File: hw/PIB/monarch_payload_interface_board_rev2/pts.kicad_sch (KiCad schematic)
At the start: 16 parts, among them U9 AD7124-8BCPZ-RL

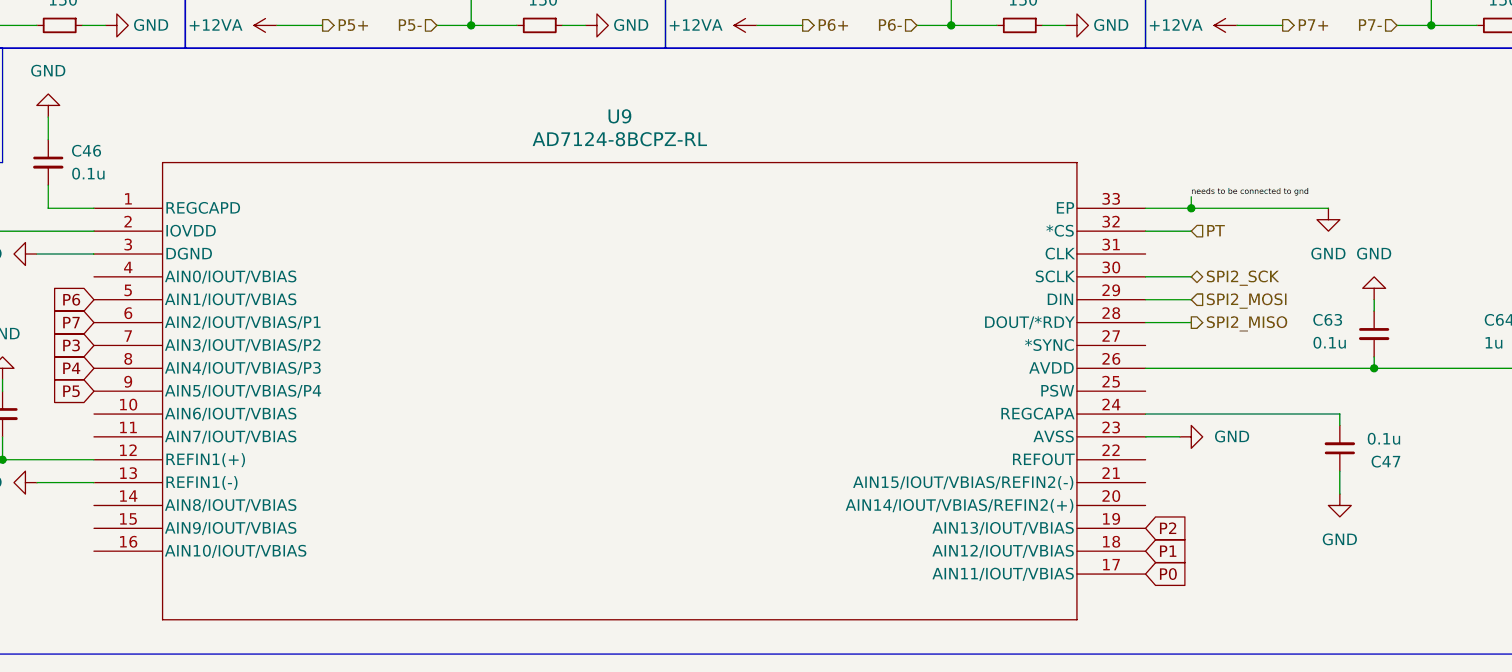
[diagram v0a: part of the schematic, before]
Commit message: Schematic Clean Up + New Micro-Lock Plus Connectors
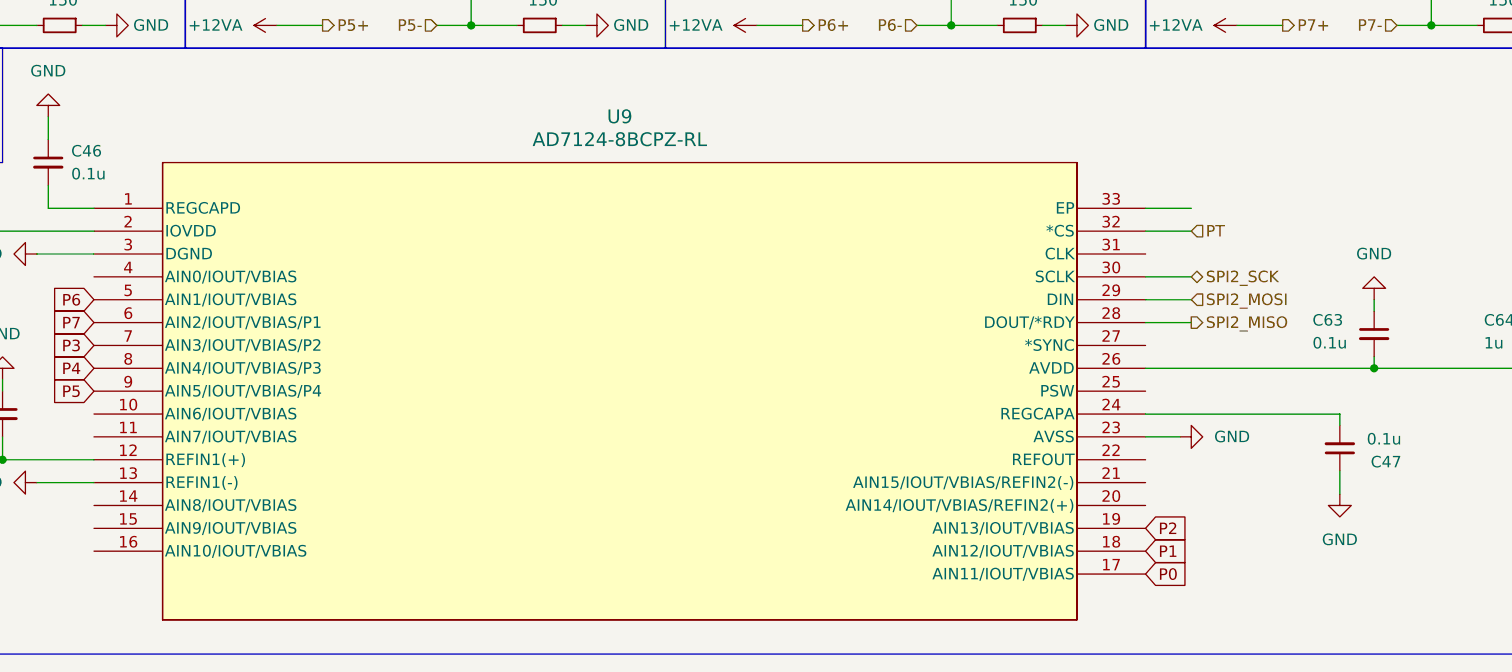
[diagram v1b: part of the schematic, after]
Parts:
- U9: footprint AD7124:CP-32-12_ADI-L -> CP-32-12_ADI
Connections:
- net GND: no longer U9.33 (EP)
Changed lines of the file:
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@@
 	)
 	(junction
-		(at 204.47 60.96)
-		(diameter 0)
-		(color 0 0 0 0)
-	)
-	(junction
 		(at 231.14 40.64)
 		(diameter 0)
@@
 	(wire
 		(pts
-			(xy 204.47 59.69) (xy 204.47 60.96)
-		)
-		(stroke
-			(width 0)
-			(type default)
-		)
-	)
-	(wire
-		(pts
 			(xy 231.14 25.4) (xy 231.14 30.48)
 		)
@@
 	(wire
 		(pts
-			(xy 204.47 60.96) (xy 219.71 60.96)
-		)
-		(stroke
-			(width 0)
-			(type default)
-		)
-	)
-	(wire
-		(pts
 			(xy 67.31 30.48) (xy 71.12 30.48)
 		)
@@
 		)
 	)
-	(label "needs to be connected to gnd"
-		(at 204.47 59.69 0)
-		(effects
-			(font
-				(size 0.635 0.635)
-			)
-			(justify left bottom)
-		)
-	)
 	(global_label "P7"
 		(shape input)
@@
 	)
 	(symbol
-		(lib_id "power:GND")
-		(at 219.71 60.96 0)
-		(unit 1)
-		(body_style 1)
-		(exclude_from_sim no)
-		(in_bom yes)
-		(on_board yes)
-		(in_pos_files yes)
-		(dnp no)
-		(fields_autoplaced yes)
-		(property "Reference" "#PWR03"
-			(at 219.71 67.31 0)
-			(hide yes)
-			(show_name no)
-			(do_not_autoplace no)
-			(effects
-				(font
-					(size 1.27 1.27)
-				)
-			)
-		)
-		(property "Value" "GND"
-			(at 219.71 66.04 0)
-			(show_name no)
-			(do_not_autoplace no)
-			(effects
-				(font
-					(size 1.27 1.27)
-				)
-			)
-		)
-		(property "Footprint" ""
-			(at 219.71 60.96 0)
-			(hide yes)
-			(show_name no)
-			(do_not_autoplace no)
-			(effects
-				(font
-					(size 1.27 1.27)
-				)
-			)
-		)
-		(property "Datasheet" ""
-			(at 219.71 60.96 0)
-			(hide yes)
-			(show_name no)
-			(do_not_autoplace no)
-			(effects
-				(font
-					(size 1.27 1.27)
-				)
-			)
-		)
-		(property "Description" "Power symbol creates a global label with name \"GND\" , ground"
-			(at 219.71 60.96 0)
-			(hide yes)
-			(show_name no)
-			(do_not_autoplace no)
-			(effects
-				(font
-					(size 1.27 1.27)
-				)
-			)
-		)
-		(pin "1"
-		)
-		(instances
-			(project "monarch_payload_interface_board_rev2"
-				(path "/bf7ee58d-ac53-49d1-a6b2-96a87d67b737/dd3c8404-7b7b-4e20-8fce-52b620531aa5"
-					(reference "#PWR03")
-					(unit 1)
-				)
-			)
-		)
-	)
-	(symbol
 		(lib_id "power:+3V3")
 		(at 248.92 78.74 270)
@@
 			)
 		)
-		(property "Footprint" "AD7124:CP-32-12_ADI-L"
+		(property "Footprint" "CP-32-12_ADI"
 			(at 82.55 60.96 0)
 			(hide yes)

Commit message: AD7124 Fixes
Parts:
- added C70: 0.1u, Capacitor_SMD:C_0603_1608Metric, symbol Device:C_Small
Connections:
- net +3V3: now also C70.1
- net GND: now also U9.33 (EP), C70.2
- no-connect marks 0 -> 10

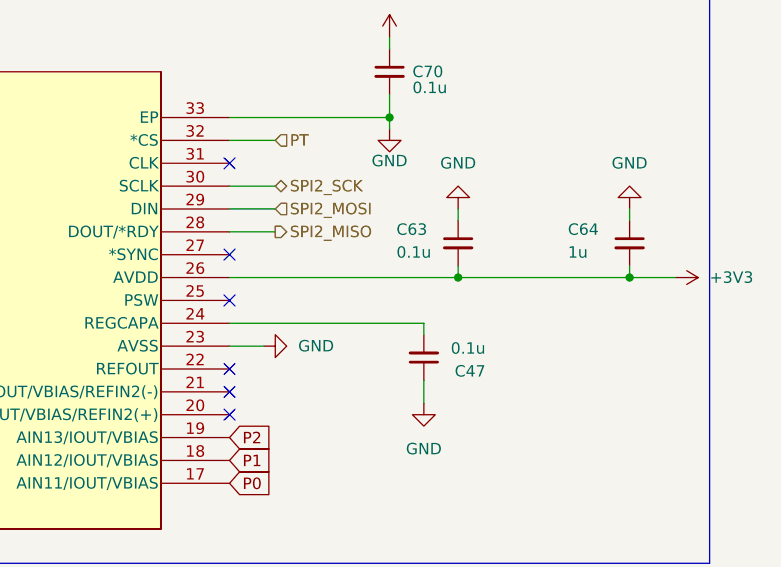
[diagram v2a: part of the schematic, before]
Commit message: Connector Footprints / Additions + Validated MAX31856
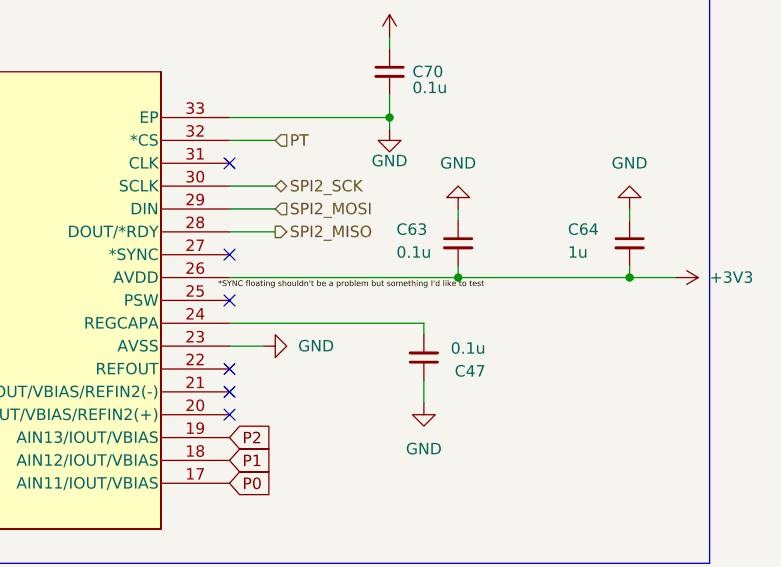
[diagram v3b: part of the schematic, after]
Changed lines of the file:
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@@
+		)
+	)
+	(label "*SYNC floating shouldn't be a problem but something I'd like to test"
+		(at 198.12 80.01 0)
+		(effects
+			(font
+				(size 0.635 0.635)
+			)
+			(justify left bottom)
 		)
 	)

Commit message: AD7124 fixes
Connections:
- net GND is gone; now on net +12VA: C46.1, C47.1, C60.1, C61.1, C62.1, C63.1, C64.1, C70.2, R32.1, R33.1, R34.1, R35.1, R36.1, R37.1, R38.1, R39.1, U9.13 (REFIN1(-)), U9.23 (AVSS), U9.3 (DGND), U9.33 (EP)
- net +12VA: now also R39.2, U9.4 (AIN0/IOUT/VBIAS), U9.5 (AIN1/IOUT/VBIAS)
- net P0: no longer R39.2
- net P6: no longer U9.5 (AIN1/IOUT/VBIAS)
- no-connect marks 10 -> 9
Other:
- moved on the sheet: R37, R39
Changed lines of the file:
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@@
 	)
 	(junction
-		(at 177.8 30.48)
+		(at 82.55 30.48)
 		(diameter 0)
 		(color 0 0 0 0)
 	)
 	(junction
-		(at 243.84 78.74)
+		(at 177.8 30.48)
 		(diameter 0)
 		(color 0 0 0 0)
 	)
 	(junction
-		(at 71.12 40.64)
+		(at 243.84 78.74)
 		(diameter 0)
 		(color 0 0 0 0)
@@
 	)
 	(junction
-		(at 124.46 40.64)
+		(at 71.12 40.64)
 		(diameter 0)
 		(color 0 0 0 0)
 	)
 	(junction
-		(at 71.12 30.48)
+		(at 124.46 40.64)
 		(diameter 0)
 		(color 0 0 0 0)
@@
 	)
 	(junction
+		(at 71.12 30.48)
+		(diameter 0)
+		(color 0 0 0 0)
+	)
+	(junction
 		(at 231.14 40.64)
 		(diameter 0)
@@
 	)
 	(no_connect
-		(at 82.55 68.58)
-	)
-	(no_connect
 		(at 82.55 96.52)
 	)
@@
 	(wire
 		(pts
+			(xy 82.55 30.48) (xy 83.82 30.48)
+		)
+		(stroke
+			(width 0)
+			(type default)
+		)
+	)
+	(wire
+		(pts
 			(xy 243.84 78.74) (xy 248.92 78.74)
 		)
@@
 	(wire
 		(pts
+			(xy 82.55 25.4) (xy 82.55 30.48)
+		)
+		(stroke
+			(width 0)
+			(type default)
+		)
+	)
+	(wire
+		(pts
 			(xy 199.39 68.58) (xy 204.47 68.58)
 		)
@@
 	(wire
 		(pts
-			(xy 71.12 30.48) (xy 76.2 30.48)
+			(xy 71.12 30.48) (xy 74.93 30.48)
 		)
 		(stroke
@@
 	(wire
 		(pts
-			(xy 81.28 30.48) (xy 83.82 30.48)
+			(xy 80.01 30.48) (xy 82.55 30.48)
 		)
 		(stroke
@@
 	(wire
 		(pts
-			(xy 71.12 40.64) (xy 76.2 40.64)
+			(xy 71.12 40.64) (xy 74.93 40.64)
 		)
 		(stroke
@@
 	(wire
 		(pts
-			(xy 81.28 40.64) (xy 83.82 40.64)
+			(xy 80.01 40.64) (xy 83.82 40.64)
 		)
 		(stroke
@@
 		)
 	)
+	(global_label "P0-"
+		(shape input)
+		(at 82.55 25.4 0)
+		(fields_autoplaced yes)
+		(effects
+			(font
+				(size 1.27 1.27)
+			)
+			(justify left)
+		)
+		(property "Intersheetrefs" "${INTERSHEET_REFS}"
+			(at 88.9329 25.4 0)
+			(hide yes)
+			(show_name no)
+			(do_not_autoplace no)
+			(effects
+				(font
+					(size 1.27 1.27)
+				)
+				(justify left)
+			)
+		)
+	)
 	(global_label "P1"
 		(shape input)
@@
 		)
 	)
+	(global_label "P0+"
+		(shape input)
+		(at 82.55 68.58 180)
+		(fields_autoplaced yes)
+		(effects
+			(font
+				(size 1.27 1.27)
+			)
+			(justify right)
+		)
+		(property "Intersheetrefs" "${INTERSHEET_REFS}"
+			(at 76.1671 68.58 0)
+			(hide yes)
+			(show_name no)
+			(do_not_autoplace no)
+			(effects
+				(font
+					(size 1.27 1.27)
+				)
+				(justify right)
+			)
+		)
+	)
 	(global_label "P6"
 		(shape input)
-		(at 82.55 71.12 180)
+		(at 76.2 71.12 180)
 		(fields_autoplaced yes)
 		(effects
@@
 		)
 		(property "Intersheetrefs" "${INTERSHEET_REFS}"
-			(at 77.0853 71.12 0)
+			(at 70.7353 71.12 0)
 			(hide yes)
 			(show_name no)
@@
 		)
 	)
-	(global_label "P0"
+	(global_label "P0-"
+		(shape input)
+		(at 82.55 71.12 180)
+		(fields_autoplaced yes)
+		(effects
+			(font
+				(size 1.27 1.27)
+			)
+			(justify right)
+		)
+		(property "Intersheetrefs" "${INTERSHEET_REFS}"
+			(at 76.1671 71.12 0)
+			(hide yes)
+			(show_name no)
+			(do_not_autoplace no)
+			(effects
+				(font
+					(size 1.27 1.27)
+				)
+				(justify right)
+			)
+		)
+	)
+	(global_label "P0+"
 		(shape input)
 		(at 71.12 25.4 180)
@@
 		)
 		(property "Intersheetrefs" "${INTERSHEET_REFS}"
-			(at 65.6553 25.4 0)
+			(at 64.7371 25.4 0)
 			(hide yes)
 			(show_name no)
@@
 	(symbol
 		(lib_id "Device:R_Small")
-		(at 78.74 30.48 270)
+		(at 77.47 30.48 270)
 		(unit 1)
 		(body_style 1)
@@
 		(dnp no)
 		(property "Reference" "R39"
-			(at 80.264 25.4 90)
+			(at 78.994 25.4 90)
 			(show_name no)
 			(do_not_autoplace no)
@@
 		)
 		(property "Value" "150"
-			(at 80.772 27.686 90)
+			(at 79.502 27.686 90)
 			(show_name no)
 			(do_not_autoplace no)
@@
 		)
 		(property "Footprint" "Resistor_SMD:R_0603_1608Metric"
-			(at 78.74 30.48 0)
+			(at 77.47 30.48 0)
 			(hide yes)
 			(show_name no)
@@
 		)
 		(property "Datasheet" ""
-			(at 78.74 30.48 0)
+			(at 77.47 30.48 0)
 			(hide yes)
 			(show_name no)
@@
 		)
 		(property "Description" "Resistor, small symbol"
-			(at 78.74 30.48 0)
+			(at 77.47 30.48 0)
 			(hide yes)
 			(show_name no)
@@
 	(symbol
 		(lib_id "Device:R_Small")
-		(at 78.74 40.64 270)
+		(at 77.47 40.64 270)
 		(unit 1)
 		(body_style 1)
@@
 		(dnp no)
 		(property "Reference" "R37"
-			(at 80.264 35.56 90)
+			(at 78.994 35.56 90)
 			(show_name no)
 			(do_not_autoplace no)
@@
 		)
 		(property "Value" "150"
-			(at 80.772 37.846 90)
+			(at 79.502 37.846 90)
 			(show_name no)
 			(do_not_autoplace no)
@@
 		)
 		(property "Footprint" "Resistor_SMD:R_0603_1608Metric"
-			(at 78.74 40.64 0)
+			(at 77.47 40.64 0)
 			(hide yes)
 			(show_name no)
@@
 		)
 		(property "Datasheet" ""
-			(at 78.74 40.64 0)
+			(at 77.47 40.64 0)
 			(hide yes)
 			(show_name no)
@@
 		)
 		(property "Description" "Resistor, small symbol"
-			(at 78.74 40.64 0)
+			(at 77.47 40.64 0)
 			(hide yes)
 			(show_name no)

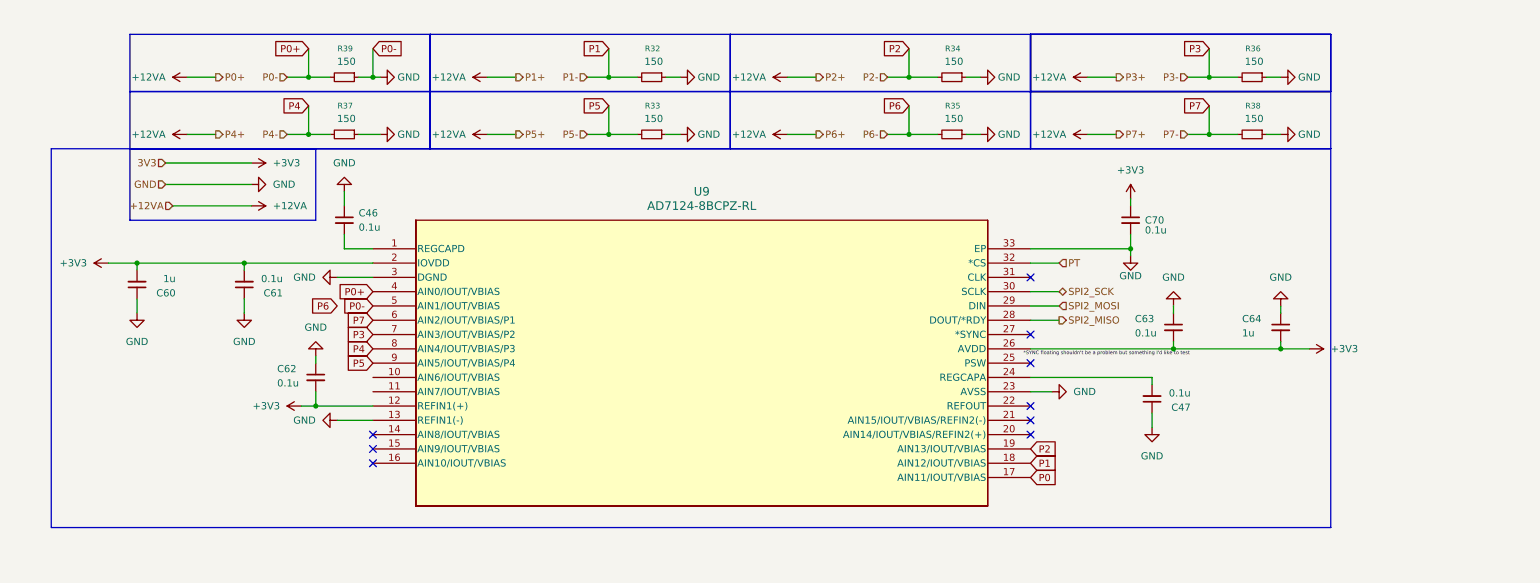
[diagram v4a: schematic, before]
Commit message: Schematic Updates Finished -> AD7124 Voltage Reading Fix + Connector Linkage Issue Fix
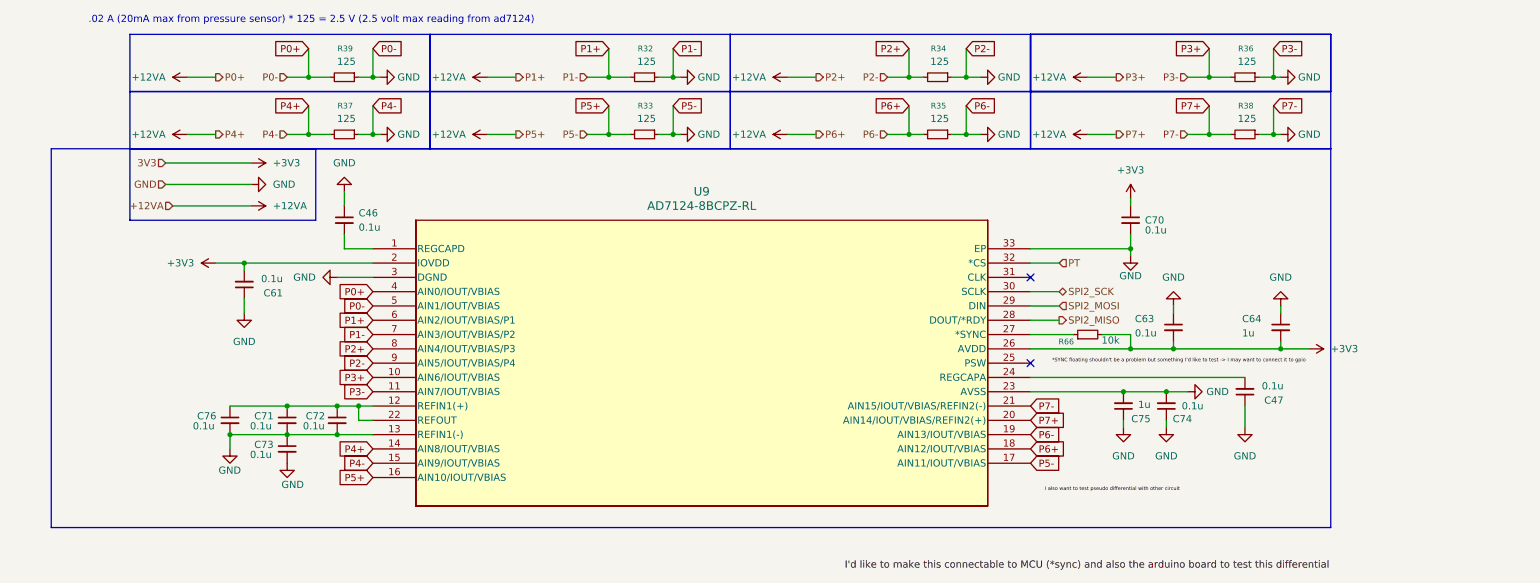
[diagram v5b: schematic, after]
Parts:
- removed C60: 1u, Capacitor_SMD:C_0603_1608Metric, symbol Device:C_Small
- removed C62: 0.1u, Capacitor_SMD:C_0603_1608Metric, symbol Device:C_Small
- added C71, C72, C73, C74, C76: 0.1u, Capacitor_SMD:C_0603_1608Metric, symbol Device:C_Small
- added C75: 1u, Capacitor_SMD:C_0603_1608Metric, symbol Device:C_Small
- added R66: 10k, Resistor_SMD:R_0603_1608Metric, symbol Device:R_Small
- R32, R33, R34, R35, R36, R37, R38, R39: value 150 -> 125
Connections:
- net P0 is gone; now on net +12VA: U9.17 (AIN11/IOUT/VBIAS)
- net P1 is gone; now on net +12VA: R32.2, U9.18 (AIN12/IOUT/VBIAS)
- net P2 is gone; now on net +12VA: R34.2, U9.19 (AIN13/IOUT/VBIAS)
- net P3 is gone; now on net +12VA: R36.2, U9.7 (AIN3/IOUT/VBIAS/P2)
- net P4 is gone; now on net +12VA: R37.2, U9.8 (AIN4/IOUT/VBIAS/P3)
- net P5 is gone; now on net +12VA: R33.2, U9.9 (AIN5/IOUT/VBIAS/P4)
- net P6 is gone; now on net +12VA: R35.2
- net P7 is gone; now on net +12VA: R38.2, U9.6 (AIN2/IOUT/VBIAS/P1)
- net +12VA: now also U9.10 (AIN6/IOUT/VBIAS), U9.11 (AIN7/IOUT/VBIAS), U9.14 (AIN8/IOUT/VBIAS), U9.15 (AIN9/IOUT/VBIAS), U9.16 (AIN10/IOUT/VBIAS), U9.20 (AIN14/IOUT/VBIAS/REFIN2(+)), U9.21 (AIN15/IOUT/VBIAS/REFIN2(-)), C71.2, C72.2, C73.1, C73.2, C74.1, C74.2, C75.1, C75.2, C76.2
- net +3V3: now also R66.2; no longer U9.12 (REFIN1(+))
- net at U9.22 (REFOUT): now also U9.12 (REFIN1(+)), C71.1, C72.1, C76.1
- net at U9.27 (*SYNC): now also R66.1
- no-connect marks 9 -> 2
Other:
- note added: ".02 A (20mA max from pressure sensor) * 125 = 2.5 V (2.5 volt max reading from ad7124)"
- moved on the sheet: C47, R32, R33, R34, R35, R36, R38

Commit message: Footprint Selected
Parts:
- U9: footprint CP-32-12_ADI -> AD7124:CP-32-12_ADI
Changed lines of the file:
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@@
 			)
 		)
-		(property "Footprint" "CP-32-12_ADI"
+		(property "Footprint" "AD7124:CP-32-12_ADI"
 			(at 82.55 60.96 0)
 			(hide yes)

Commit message: Initial Routing Work + Placement
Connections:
- net +12VA: no longer C46.1, C47.1, C61.1, C63.1, C64.1, C70.2, C71.2, C72.2, C73.1, C73.2, C74.1, C74.2, C75.1, C75.2, C76.2, R32.1, R32.2, R33.1, R33.2, R34.1, R34.2, R35.1, R35.2, R36.1, R36.2, R37.1, R37.2, R38.1, R38.2, R39.1, R39.2, U9.10 (AIN6/IOUT/VBIAS), U9.11 (AIN7/IOUT/VBIAS), U9.13 (REFIN1(-)), U9.14 (AIN8/IOUT/VBIAS), U9.15 (AIN9/IOUT/VBIAS), U9.16 (AIN10/IOUT/VBIAS), U9.17 (AIN11/IOUT/VBIAS), U9.18 (AIN12/IOUT/VBIAS), U9.19 (AIN13/IOUT/VBIAS), U9.20 (AIN14/IOUT/VBIAS/REFIN2(+)), U9.21 (AIN15/IOUT/VBIAS/REFIN2(-)), U9.23 (AVSS), U9.3 (DGND), U9.33 (EP), U9.4 (AIN0/IOUT/VBIAS), U9.5 (AIN1/IOUT/VBIAS), U9.6 (AIN2/IOUT/VBIAS/P1), U9.7 (AIN3/IOUT/VBIAS/P2), U9.8 (AIN4/IOUT/VBIAS/P3), U9.9 (AIN5/IOUT/VBIAS/P4)
- new net GND: C46.1, C47.1, C61.1, C63.1, C64.1, C70.2, C71.2, C72.2, C73.1, C73.2, C74.1, C74.2, C75.1, C75.2, C76.2, R32.1, R33.1, R34.1, R35.1, R36.1, R37.1, R38.1, R39.1, U9.11 (AIN7/IOUT/VBIAS), U9.13 (REFIN1(-)), U9.15 (AIN9/IOUT/VBIAS), U9.17 (AIN11/IOUT/VBIAS), U9.19 (AIN13/IOUT/VBIAS), U9.21 (AIN15/IOUT/VBIAS/REFIN2(-)), U9.23 (AVSS), U9.3 (DGND), U9.33 (EP), U9.5 (AIN1/IOUT/VBIAS), U9.7 (AIN3/IOUT/VBIAS/P2), U9.9 (AIN5/IOUT/VBIAS/P4)
- new net P0REF+: R39.2, U9.4 (AIN0/IOUT/VBIAS)
- new net P1REF+: R32.2, U9.6 (AIN2/IOUT/VBIAS/P1)
- new net P2REF+: R34.2, U9.8 (AIN4/IOUT/VBIAS/P3)
- new net P3REF+: R36.2, U9.10 (AIN6/IOUT/VBIAS)
- new net P4REF+: R37.2, U9.14 (AIN8/IOUT/VBIAS)
- new net P5REF+: R33.2, U9.16 (AIN10/IOUT/VBIAS)
- new net P6REF+: R35.2, U9.18 (AIN12/IOUT/VBIAS)
- new net P7REF+: R38.2, U9.20 (AIN14/IOUT/VBIAS/REFIN2(+))
